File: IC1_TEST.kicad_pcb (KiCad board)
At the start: 4 copper layers, 26 parts, among them IC1 ADM3054WBRWZ-RL7-!my_lib, J1 B4B-XH-A_LF__SN_-!my_lib, SW1 SW_DIP_x03, SW2 SW_Push, U1 DEV-16771, U2 MAX6369KA+T

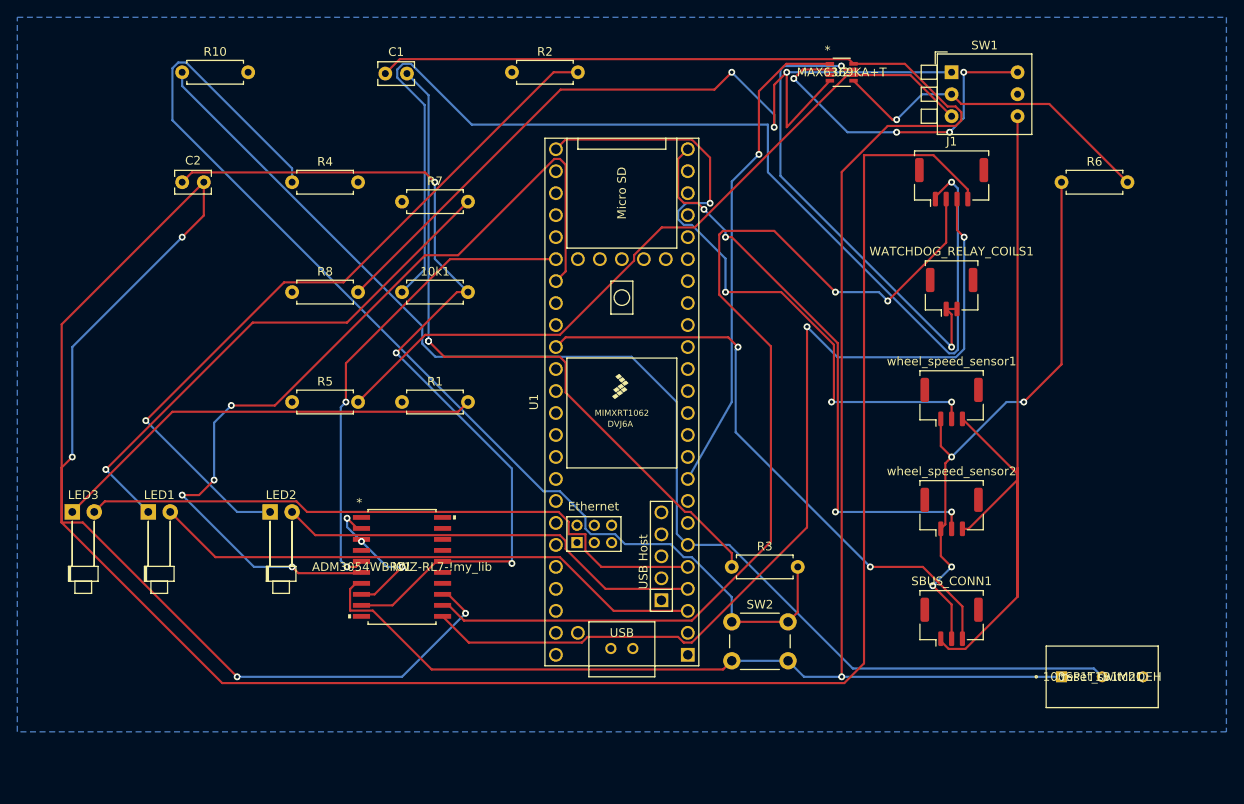
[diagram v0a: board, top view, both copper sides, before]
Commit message: pcb changes
changed connectors, redid wire paths
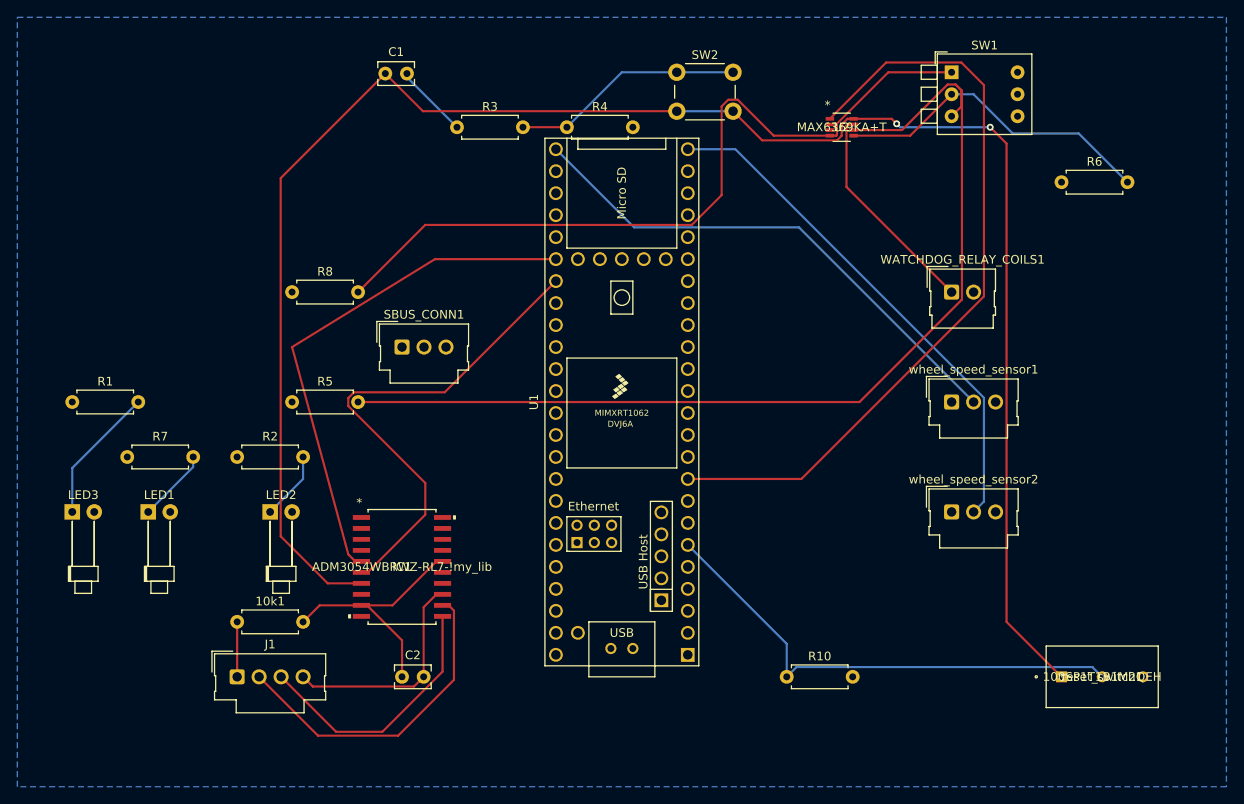
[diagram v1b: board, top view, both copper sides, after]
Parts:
- J1: footprint Connector_Molex:Molex_CLIK-Mate_502382-0470_1x04-1MP_P1.25mm_Vertical -> Connector_Molex:Molex_SL_171971-0004_1x04_P2.54mm_Vertical
- SBUS_CONN1, wheel_speed_sensor1, wheel_speed_sensor2: footprint Connector_Molex:Molex_CLIK-Mate_502382-0370_1x03-1MP_P1.25mm_Vertical -> Connector_Molex:Molex_SL_171971-0003_1x03_P2.54mm_Vertical
- WATCHDOG_RELAY_COILS1: footprint Connector_Molex:Molex_CLIK-Mate_502382-0270_1x02-1MP_P1.25mm_Vertical -> Connector_Molex:Molex_SL_171971-0002_1x02_P2.54mm_Vertical
- moved J1 100.4 mm to (120.7, 158.8)
- moved R10 98.8 mm to (184.2, 158.8)
- moved SBUS_CONN1 71.0 mm to (139.7, 120.7)
- moved SW2 63.8 mm to (171.4, 88.9)
- moved C2 62.5 mm to (139.7, 158.8)
- moved R3 59.9 mm to (146.1, 95.2)
- moved R2 54.6 mm to (120.7, 133.3)
- moved R7 43.3 mm to (108.0, 133.3)
- moved 10k1 42.6 mm to (120.7, 152.4)
- moved R1 38.1 mm to (101.6, 127.0)
- moved R4 32.4 mm to (158.8, 95.2)
- moved U2 6.35 mm to (190.5, 95.2)
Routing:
- net ODRIVE_5V+: track 327.8 -> 25.7 mm, vias 4 -> 0
- net GNDREF: track 157.2 -> 0.00 mm, vias 7 -> 0
- net Net-(10k1-Pad1): track 132.9 -> 6.35 mm, vias 1 -> 0
- net Net-(R3-Pad2): track 131.2 -> 26.9 mm
- net DIO_BUTTON: track 146.3 -> 57.4 mm
- net CAN_H: track 118.0 -> 37.6 mm, vias 2 -> 0
- net CAN_L: track 110.3 -> 30.6 mm, vias 2 -> 0
- net Net-(LED2-Pad1): track 85.3 -> 7.93 mm, vias 1 -> 0
- net ODRIVE_GND: track 105.1 -> 29.6 mm, vias 3 -> 0
- net Net-(C1-Pad2): track 80.7 -> 8.59 mm, vias 2 -> 0
- net +5V: track 66.9 -> 0.00 mm, vias 4 -> 0
- net SBUS: track 70.2 -> 12.7 mm, vias 2 -> 0
- net Net-(LED1-Pad1): track 61.6 -> 8.50 mm, vias 1 -> 0
- net CTX: track 103.0 -> 56.9 mm, vias 4 -> 0
- net Net-(LED3-Pad1): track 51.0 -> 15.9 mm
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
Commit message: pcb changes
moved R5, redid wire routing
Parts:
- moved R5 78.5 mm to (203.2, 108.0), turned to 90 degrees
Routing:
- net SET2: track 118.2 -> 24.7 mm
- net CRX: track 60.0 -> 51.3 mm
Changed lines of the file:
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@@
   )
   (footprint "Resistor_THT:R_Axial_DIN0207_L6.3mm_D2.5mm_P7.62mm_Horizontal" (layer "F.Cu")
-    (at 127 127)
+    (at 203.2 107.95 90)
     (descr "Resistor, Axial_DIN0207 series, Axial, Horizontal, pin pitch=7.62mm, 0.25W = 1/4W, length*diameter=6.3*2.5mm^2, http://cdn-reichelt.de/documents/datenblatt/B400/1_4W%23YAG.pdf")
     (tags "Resistor Axial_DIN0207 series Axial Horizontal pin pitch 7.62mm 0.25W = 1/4W length 6.3mm diameter 2.5mm")
@@
     (property "Sheetname" "")
     (attr through_hole)
-    (fp_text reference "R5" (at 3.81 -2.37) (layer "F.SilkS")
-      (effects (font (size 1 1) (thickness 0.15)))
-    )
-    (fp_text value "R_US" (at 3.81 2.37) (layer "F.Fab")
-      (effects (font (size 1 1) (thickness 0.15)))
-    )
-    (fp_text user "${REFERENCE}" (at 3.81 0) (layer "F.Fab")
+    (fp_text reference "R5" (at 3.81 -2.37 90) (layer "F.SilkS")
+      (effects (font (size 1 1) (thickness 0.15)))
+    )
+    (fp_text value "R_US" (at 3.81 2.37 90) (layer "F.Fab")
+      (effects (font (size 1 1) (thickness 0.15)))
+    )
+    (fp_text user "${REFERENCE}" (at 3.81 0 90) (layer "F.Fab")
       (effects (font (size 1 1) (thickness 0.15)))
     )
@@
     (fp_line (start 0.66 -1.25) (end 0.66 1.25) (layer "F.Fab") (width 0.1))
     (fp_line (start 0.66 1.25) (end 6.96 1.25) (layer "F.Fab") (width 0.1))
-    (pad "1" thru_hole circle (at 0 0) (size 1.6 1.6) (drill 0.8) (layers *.Cu *.Mask)
+    (pad "1" thru_hole circle (at 0 0 90) (size 1.6 1.6) (drill 0.8) (layers *.Cu *.Mask)
       (net 57 "+5V") (pintype "passive"))
-    (pad "2" thru_hole oval (at 7.62 0) (size 1.6 1.6) (drill 0.8) (layers *.Cu *.Mask)
+    (pad "2" thru_hole oval (at 7.62 0 90) (size 1.6 1.6) (drill 0.8) (layers *.Cu *.Mask)
       (net 6 "SET2") (pintype "passive"))
     (model "${KICAD6_3DMODEL_DIR}/Resistor_THT.3dshapes/R_Axial_DIN0207_L6.3mm_D2.5mm_P7.62mm_Horizontal.wrl"
@@
   (segment (start 217.894511 95.974511) (end 210.274511 95.974511) (width 0.25) (layer "B.Cu") (net 5))
   (segment (start 210.274511 95.974511) (end 205.74 91.44) (width 0.25) (layer "B.Cu") (net 5))
+  (segment (start 191.865948 95.575001) (end 197.474699 95.575001) (width 0.25) (layer "F.Cu") (net 6))
+  (segment (start 203.2 93.98) (end 203.2 100.33) (width 0.25) (layer "F.Cu") (net 6))
+  (segment (start 203.665789 90.315489) (end 204.324511 90.974211) (width 0.25) (layer "F.Cu") (net 6))
   (segment (start 202.734211 90.315489) (end 203.665789 90.315489) (width 0.25) (layer "F.Cu") (net 6))
+  (segment (start 197.474699 95.575001) (end 202.734211 90.315489) (width 0.25) (layer "F.Cu") (net 6))
   (segment (start 204.324511 92.855489) (end 203.2 93.98) (width 0.25) (layer "F.Cu") (net 6))
-  (segment (start 191.865948 95.575001) (end 197.474699 95.575001) (width 0.25) (layer "F.Cu") (net 6))
-  (segment (start 204.39452 115.157973) (end 192.552493 127) (width 0.25) (layer "F.Cu") (net 6))
   (segment (start 204.324511 90.974211) (end 204.324511 92.855489) (width 0.25) (layer "F.Cu") (net 6))
-  (segment (start 204.39452 91.04422) (end 204.39452 115.157973) (width 0.25) (layer "F.Cu") (net 6))
-  (segment (start 197.474699 95.575001) (end 202.734211 90.315489) (width 0.25) (layer "F.Cu") (net 6))
-  (segment (start 192.552493 127) (end 134.62 127) (width 0.25) (layer "F.Cu") (net 6))
-  (segment (start 203.665789 90.315489) (end 204.39452 91.04422) (width 0.25) (layer "F.Cu") (net 6))
-  (segment (start 203.665789 90.315489) (end 204.324511 90.974211) (width 0.25) (layer "F.Cu") (net 6))
   (segment (start 191.051787 102.151787) (end 203.2 114.3) (width 0.25) (layer "F.Cu") (net 7))
   (segment (start 191.865948 94.924999) (end 191.161378 94.924999) (width 0.25) (layer "F.Cu") (net 7))
@@
   (segment (start 144.634511 125.875489) (end 157.48 113.03) (width 0.25) (layer "F.Cu") (net 31))
   (segment (start 142.3896 136.3599) (end 133.495489 127.465789) (width 0.25) (layer "F.Cu") (net 31))
-  (segment (start 127 120.65) (end 143.51 110.49) (width 0.25) (layer "F.Cu") (net 32))
+  (segment (start 133.045969 126.348014) (end 137.156842 122.237141) (width 0.25) (layer "F.Cu") (net 32))
+  (segment (start 145.732859 122.237141) (end 157.48 110.49) (width 0.25) (layer "F.Cu") (net 32))
+  (segment (start 137.156842 122.237141) (end 145.732859 122.237141) (width 0.25) (layer "F.Cu") (net 32))
+  (segment (start 133.045969 144.158469) (end 133.045969 126.348014) (width 0.25) (layer "F.Cu") (net 32))
   (segment (start 135.0137 145.415) (end 134.3025 145.415) (width 0.25) (layer "F.Cu") (net 32))
-  (segment (start 134.3025 145.415) (end 133.495489 144.607989) (width 0.25) (layer "F.Cu") (net 32))
-  (segment (start 143.51 110.49) (end 157.48 110.49) (width 0.25) (layer "F.Cu") (net 32))
-  (segment (start 133.495489 144.607989) (end 127 120.65) (width 0.25) (layer "F.Cu") (net 32))
+  (segment (start 134.3025 145.415) (end 133.045969 144.158469) (width 0.25) (layer "F.Cu") (net 32))
   (segment (start 166.515489 106.825489) (end 157.48 97.79) (width 0.25) (layer "B.Cu") (net 37))
   (segment (start 205.74 127) (end 185.565489 106.825489) (width 0.25) (layer "B.Cu") (net 37))

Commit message: connected to gndref on chips
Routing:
- net GNDREF: track 0.00 -> 21.7 mm, vias 0 -> 3
- net WATCHDOG_OUTPUT: track 25.2 -> 27.7 mm
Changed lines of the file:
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@@
   (segment (start 206.934511 114.794784) (end 185.839295 135.89) (width 0.25) (layer "F.Cu") (net 1))
   (segment (start 189.134052 94.275001) (end 195.633564 87.775489) (width 0.25) (layer "F.Cu") (net 1))
+  (segment (start 135.0137 142.875) (end 136.525 142.875) (width 0.25) (layer "F.Cu") (net 2))
+  (segment (start 135.0137 149.225) (end 137.863402 149.225) (width 0.25) (layer "F.Cu") (net 2))
+  (segment (start 137.863402 149.225) (end 138.351952 149.71355) (width 0.25) (layer "F.Cu") (net 2))
+  (segment (start 135.0137 141.605) (end 137.441054 141.605) (width 0.25) (layer "F.Cu") (net 2))
+  (segment (start 184.475001 94.924999) (end 184.15 95.25) (width 0.25) (layer "F.Cu") (net 2))
+  (segment (start 136.525 142.875) (end 140.070554 139.329446) (width 0.25) (layer "F.Cu") (net 2))
+  (segment (start 189.134052 94.924999) (end 184.475001 94.924999) (width 0.25) (layer "F.Cu") (net 2))
+  (segment (start 140.070554 139.329446) (end 140.070554 138.9755) (width 0.25) (layer "F.Cu") (net 2))
+  (segment (start 137.441054 141.605) (end 140.070554 138.9755) (width 0.25) (layer "F.Cu") (net 2))
+  (via (at 184.15 95.25) (size 0.8) (drill 0.4) (layers "F.Cu" "B.Cu") (net 2))
+  (via (at 138.351952 149.71355) (size 0.8) (drill 0.4) (layers "F.Cu" "B.Cu") (net 2))
+  (via (at 140.070554 138.9755) (size 0.8) (drill 0.4) (layers "F.Cu" "B.Cu") (net 2))
   (segment (start 195.886377 88.9) (end 189.948213 94.838164) (width 0.25) (layer "F.Cu") (net 4))
   (segment (start 189.873702 96.224999) (end 189.134052 96.224999) (width 0.25) (layer "F.Cu") (net 4))
@@
   (segment (start 191.051787 95.03459) (end 191.051787 102.151787) (width 0.25) (layer "F.Cu") (net 7))
   (segment (start 191.161378 94.924999) (end 191.051787 95.03459) (width 0.25) (layer "F.Cu") (net 7))
+  (segment (start 205.74 114.3) (end 203.2 114.3) (width 0.25) (layer "F.Cu") (net 7))
   (segment (start 196.85 94.850501) (end 196.2745 94.275001) (width 0.25) (layer "F.Cu") (net 8))
   (segment (start 209.55 97.140989) (end 207.659011 95.25) (width 0.25) (layer "F.Cu") (net 8))

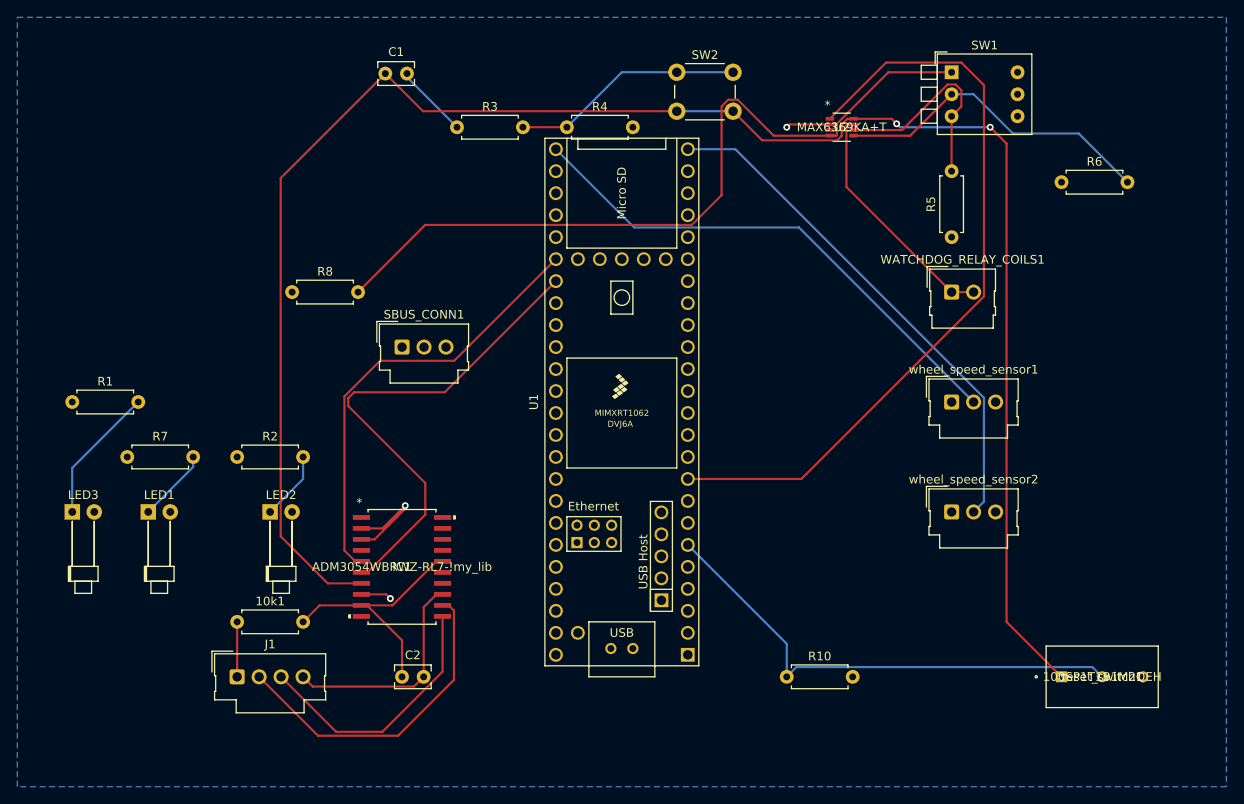
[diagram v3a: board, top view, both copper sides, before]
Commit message: no more overlapping w/ pads, finished teensy pins
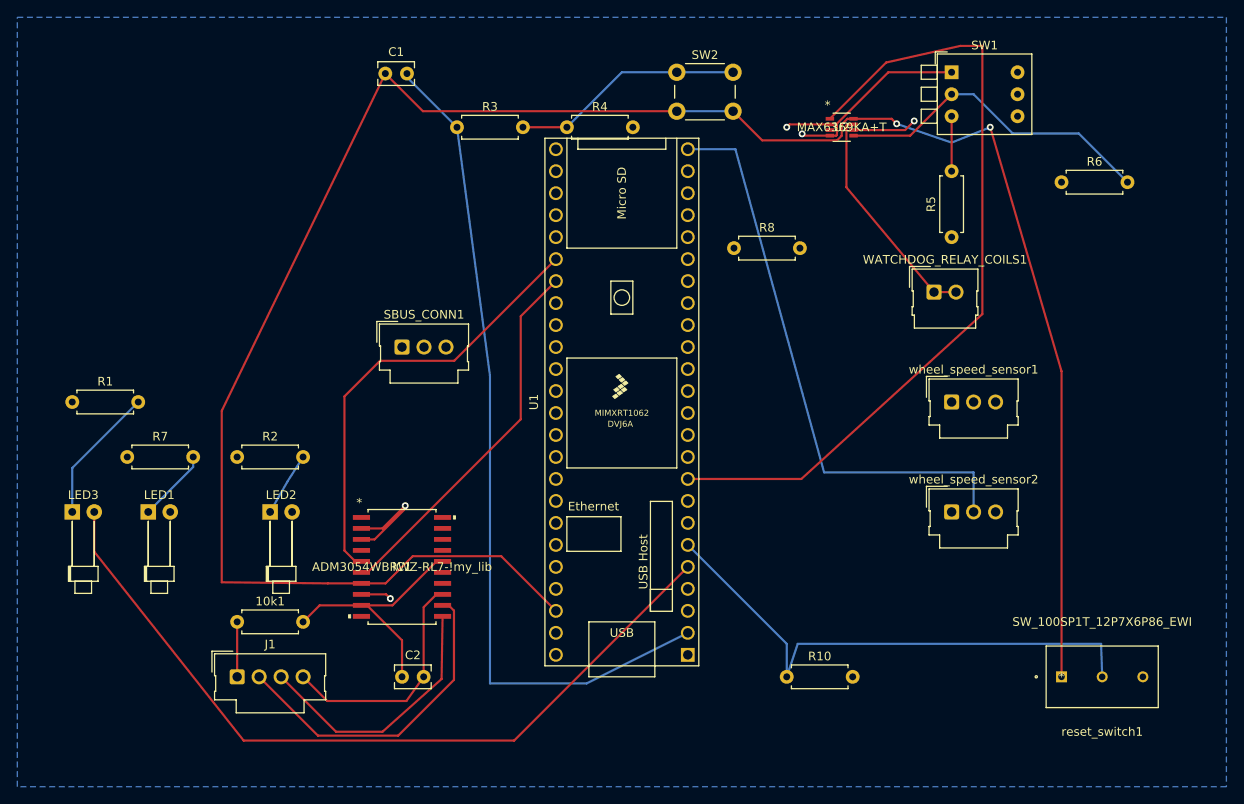
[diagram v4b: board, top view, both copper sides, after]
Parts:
- reset_switch1: value 100SP1T1B1M2QEH -> SW_100SP1T_12P7X6P86_EWI
- moved R8 51.3 mm to (178.1, 109.2)
- moved WATCHDOG_RELAY_COILS1 2.03 mm to (201.2, 114.3)
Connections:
- C1 pad 2: Net-(C1-Pad2) -> DIO_SWITCH
- R3 pad 1: Net-(C1-Pad2) -> DIO_SWITCH
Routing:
- net DIO_SWITCH: track 0.00 -> 97.3 mm
- net SET0: track 89.3 -> 34.5 mm, vias 0 -> 1
- net 3.3v_SUPPLY: track 212.2 -> 246.1 mm
- net LED1: track 64.5 -> 94.1 mm
- net LED2: track 49.4 -> 70.0 mm
- net LED3: track 75.9 -> 92.0 mm
- net CTX: track 56.9 -> 43.4 mm
- net wheel_speed_sensor1: track 60.4 -> 73.5 mm
- net Net-(C1-Pad2): track 8.59 -> 0.00 mm
- net SET2: track 24.7 -> 18.3 mm, vias 0 -> 1
- net wheel_speed_sensor2: track 59.8 -> 66.1 mm
- net DIO_BUTTON: track 57.4 -> 62.9 mm
- net DIO_WATCHDOG: track 88.9 -> 92.9 mm
- net ODRIVE_5V+: track 25.7 -> 27.4 mm
- net WATCHDOG_OUTPUT: track 27.7 -> 26.4 mm
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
